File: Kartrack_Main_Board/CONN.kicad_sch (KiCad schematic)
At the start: 17 parts, among them J1 USB_C_Receptacle_USB2.0_14P, SW1 SW_Push, SW2 SW_Push, SW3 SW_Push

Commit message: pcb
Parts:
- added VEXTD1: Conn_01x02_Socket, Connector_Phoenix_MC:PhoenixContact_MC_1,5_2-G-3.81_1x02_P3.81mm_Horizontal, symbol Connector:Conn_01x02_Socket
- JP1: footprint (none) -> Jumper:SolderJumper-2_P1.3mm_Open_RoundedPad1.0x1.5mm
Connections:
- net GND: now also VEXTD1.2 (Pin_2)
- net at JP1.2 (B): now also VEXTD1.1 (Pin_1)
- net PF6_STBY_GPS renamed PF6
- net PG6 renamed PG6_STBY_GPS
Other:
- note added: "VEXT DISCO"
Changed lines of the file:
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@@
 		)
 	)
+	(text "VEXT DISCO\n"
+		(exclude_from_sim no)
+		(at 184.912 44.196 0)
+		(effects
+			(font
+				(size 1.27 1.27)
+			)
+		)
+	)
 	(junction
 		(at 55.88 113.03)
@@
 	(wire
 		(pts
-			(xy 186.69 54.61) (xy 186.69 55.88)
+			(xy 186.69 53.34) (xy 186.69 55.88)
 		)
 		(stroke
@@
 	(wire
 		(pts
+			(xy 179.07 53.34) (xy 186.69 53.34)
+		)
+		(stroke
+			(width 0)
+			(type default)
+		)
+	)
+	(wire
+		(pts
+			(xy 179.07 50.8) (xy 190.5 50.8)
+		)
+		(stroke
+			(width 0)
+			(type default)
+		)
+	)
+	(wire
+		(pts
 			(xy 194.31 57.15) (xy 194.31 66.04)
 		)
@@
 	(wire
 		(pts
+			(xy 190.5 50.8) (xy 190.5 52.07)
+		)
+		(stroke
+			(width 0)
+			(type default)
+		)
+	)
+	(wire
+		(pts
 			(xy 161.29 154.94) (xy 161.29 153.67)
 		)
@@
 		)
 	)
-	(hierarchical_label "PF6_STBY_GPS"
+	(hierarchical_label "PF6"
 		(shape input)
 		(at 201.93 104.14 0)
@@
 		)
 	)
-	(hierarchical_label "PG6"
+	(hierarchical_label "PG6_STBY_GPS"
 		(shape input)
 		(at 176.53 81.28 180)
@@
 	)
 	(symbol
+		(lib_id "Connector:Conn_01x02_Socket")
+		(at 173.99 53.34 180)
+		(unit 1)
+		(exclude_from_sim no)
+		(in_bom yes)
+		(on_board yes)
+		(dnp no)
+		(fields_autoplaced yes)
+		(property "Reference" "VEXTD1"
+			(at 174.625 45.72 0)
+			(effects
+				(font
+					(size 1.27 1.27)
+				)
+			)
+		)
+		(property "Value" "Conn_01x02_Socket"
+			(at 174.625 48.26 0)
+			(effects
+				(font
+					(size 1.27 1.27)
+				)
+			)
+		)
+		(property "Footprint" "Connector_Phoenix_MC:PhoenixContact_MC_1,5_2-G-3.81_1x02_P3.81mm_Horizontal"
+			(at 173.99 53.34 0)
+			(effects
+				(font
+					(size 1.27 1.27)
+				)
+				(hide yes)
+			)
+		)
+		(property "Datasheet" "~"
+			(at 173.99 53.34 0)
+			(effects
+				(font
+					(size 1.27 1.27)
+				)
+				(hide yes)
+			)
+		)
+		(property "Description" "Generic connector, single row, 01x02, script generated"
+			(at 173.99 53.34 0)
+			(effects
+				(font
+					(size 1.27 1.27)
+				)
+				(hide yes)
+			)
+		)
+		(pin "2"
+		)
+		(pin "1"
+		)
+		(instances
+			(project ""
+				(path "/7d0ecb76-dd3a-488e-b45e-ae217463e751/85ccdc23-ae17-49a7-b6f3-41d41d1b2e3d"
+					(reference "VEXTD1")
+					(unit 1)
+				)
+			)
+		)
+	)
+	(symbol
 		(lib_id "power:+3.3V")
 		(at 204.47 133.35 0)
@@
 	)
 	(symbol
-		(lib_id "power:VDD")
-		(at 186.69 54.61 0)
-		(unit 1)
-		(exclude_from_sim no)
-		(in_bom yes)
-		(on_board yes)
-		(dnp no)
-		(fields_autoplaced yes)
-		(property "Reference" "#PWR04"
-			(at 186.69 58.42 0)
-			(effects
-				(font
-					(size 1.27 1.27)
-				)
-				(hide yes)
-			)
-		)
-		(property "Value" "VEXT_DISCO"
-			(at 186.69 49.53 0)
-			(effects
-				(font
-					(size 1.27 1.27)
-				)
-			)
-		)
-		(property "Footprint" ""
-			(at 186.69 54.61 0)
-			(effects
-				(font
-					(size 1.27 1.27)
-				)
-				(hide yes)
-			)
-		)
-		(property "Datasheet" ""
-			(at 186.69 54.61 0)
-			(effects
-				(font
-					(size 1.27 1.27)
-				)
-				(hide yes)
-			)
-		)
-		(property "Description" "Power symbol creates a global label with name \"VDD\""
-			(at 186.69 54.61 0)
-			(effects
-				(font
-					(size 1.27 1.27)
-				)
-				(hide yes)
-			)
-		)
-		(pin "1"
-		)
-		(instances
-			(project ""
-				(path "/7d0ecb76-dd3a-488e-b45e-ae217463e751/85ccdc23-ae17-49a7-b6f3-41d41d1b2e3d"
-					(reference "#PWR04")
-					(unit 1)
-				)
-			)
-		)
-	)
-	(symbol
 		(lib_id "MCU_Module:Arduino_UNO_R3")
 		(at 189.23 91.44 0)
@@
 			)
 		)
-		(property "Footprint" ""
+		(property "Footprint" "Jumper:SolderJumper-2_P1.3mm_Open_RoundedPad1.0x1.5mm"
 			(at 186.69 59.69 0)
 			(effects
@@
 					(unit 1)
 				)
+			)
+		)
+	)
+	(symbol
+		(lib_id "power:GND")
+		(at 190.5 52.07 0)
+		(unit 1)
+		(exclude_from_sim no)
+		(in_bom yes)
+		(on_board yes)
+		(dnp no)
+		(fields_autoplaced yes)
+		(property "Reference" "#PWR04"
+			(at 190.5 58.42 0)
+			(effects
+				(font
+					(size 1.27 1.27)
+				)
+				(hide yes)
+			)
+		)
+		(property "Value" "GND"
+			(at 190.5 57.15 0)
+			(effects
+				(font
+					(size 1.27 1.27)
+				)
+			)
+		)
+		(property "Footprint" ""
+			(at 190.5 52.07 0)
+			(effects
+				(font
+					(size 1.27 1.27)
+				)
+				(hide yes)
+			)
+		)
+		(property "Datasheet" ""
+			(at 190.5 52.07 0)
+			(effects
+				(font
+					(size 1.27 1.27)
+				)
+				(hide yes)
+			)
+		)
+		(property "Description" "Power symbol creates a global label with name \"GND\" , ground"
+			(at 190.5 52.07 0)
+			(effects
+				(font
+					(size 1.27 1.27)
+				)
+				(hide yes)
+			)
+		)
+		(pin "1"
+		)
+		(instances
+			(project ""
+				(path "/7d0ecb76-dd3a-488e-b45e-ae217463e751/85ccdc23-ae17-49a7-b6f3-41d41d1b2e3d"
+					(reference "#PWR04")
+					(unit 1)
+				)

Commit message: PCB V1
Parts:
- removed J1: USB_C_Receptacle_USB2.0_14P, Connector_USB:USB_C_Receptacle_GCT_USB4125-xx-x-0190_6P_TopMnt_Horizontal, symbol Connector:USB_C_Receptacle_USB2.0_14P
- added J6: USB_C_Receptacle_PowerOnly_6P, Connector_USB:USB_C_Receptacle_GCT_USB4125-xx-x_6P_TopMnt_Horizontal, symbol Connector:USB_C_Receptacle_PowerOnly_6P
- added JP3: SolderJumper_2_Open, Jumper:SolderJumper-2_P1.3mm_Open_RoundedPad1.0x1.5mm, symbol Jumper:SolderJumper_2_Open
- SW1, SW2, SW3: footprint Connector_PinSocket_2.54mm:PinSocket_1x02_P2.54mm_Vertical_SMD_Pin1Left -> Connector_JST:JST_PH_S2B-PH-K_1x02_P2.00mm_Horizontal
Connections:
- net +5V: now also J6.A9 (VBUS), J6.B9 (VBUS), JP3.2 (B); no longer A2.5 (+5V)
- net GND: now also J6.A12 (GND), J6.B12 (GND), J6.S1 (SHIELD)
- net at R1.1: now also J6.A5 (CC1)
- net at R2.1: now also J6.B5 (CC2)
- new net: A2.5 (+5V), JP3.1 (A)
- no-connect marks 10 -> 6
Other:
- moved on the sheet: R1, R2

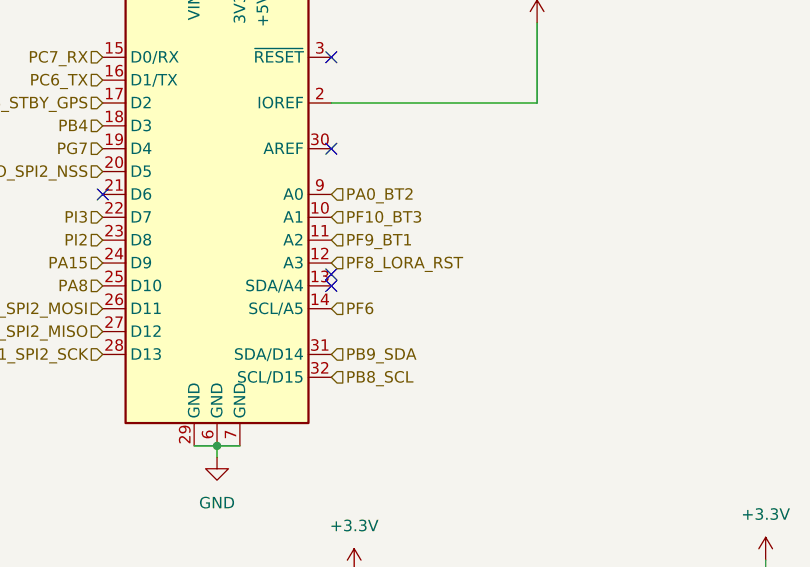
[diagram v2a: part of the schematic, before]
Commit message: add adc batt
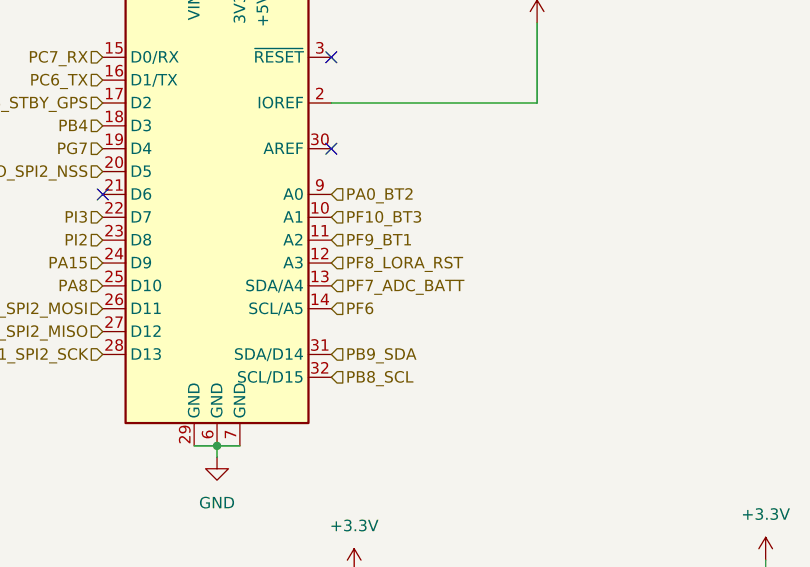
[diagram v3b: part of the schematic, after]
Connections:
- net PF7_ADC_BATT: now reaches A2.13 (SDA/A4)
- no-connect marks 6 -> 4
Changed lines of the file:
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@@
-	)
-	(no_connect
-		(at 201.93 101.6)
 	)
 	(no_connect
 		(at 201.93 86.36)
-	)
-	(no_connect
-		(at 201.93 100.33)
 	)
 	(wire
@@
 		(effects
 			(font
+				(size 1.27 1.27)
+			)
+			(justify left)
+		)
+	)
+	(hierarchical_label "PF7_ADC_BATT"
+		(shape input)
+		(at 201.93 101.6 0)
+		(effects
+			(font

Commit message: Alim jumper
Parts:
- removed JP3: SolderJumper_2_Open, Jumper:SolderJumper-2_P1.3mm_Open_RoundedPad1.0x1.5mm, symbol Jumper:SolderJumper_2_Open
- added JP4: SolderJumper_3_Open, Jumper:SolderJumper-3_P2.0mm_Open_TrianglePad1.0x1.5mm_NumberLabels, symbol Jumper:SolderJumper_3_Open
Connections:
- net +5V: now also JP4.1 (A)
- net at A2.5 (+5V): now also JP4.3 (B)
- net at A2.8 (VIN), JP1.1 (A): now also JP4.2 (C)
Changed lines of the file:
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@@
+	)
+	(junction
+		(at 186.69 64.77)
+		(diameter 0)
+		(color 0 0 0 0)
 	)
 	(junction
@@
 	(wire
 		(pts
+			(xy 186.69 64.77) (xy 190.5 64.77)
+		)
+		(stroke
+			(width 0)
+			(type default)
+		)
+	)
+	(wire
+		(pts
 			(xy 229.87 142.24) (xy 236.22 142.24)
 		)
@@
 	(wire
 		(pts
+			(xy 186.69 64.77) (xy 186.69 66.04)
+		)
+		(stroke
+			(width 0)
+			(type default)
+		)
+	)
+	(wire
+		(pts
 			(xy 142.24 142.24) (xy 147.32 142.24)
 		)
@@
 	(wire
 		(pts
+			(xy 194.31 64.77) (xy 194.31 66.04)
+		)
+		(stroke
+			(width 0)
+			(type default)
+		)
+	)
+	(wire
+		(pts
 			(xy 189.23 119.38) (xy 189.23 120.65)
 		)
@@
 	(wire
 		(pts
-			(xy 194.31 50.8) (xy 194.31 55.88)
+			(xy 186.69 63.5) (xy 186.69 64.77)
 		)
 		(stroke
@@
 	(wire
 		(pts
+			(xy 190.5 59.69) (xy 190.5 64.77)
+		)
+		(stroke
+			(width 0)
+			(type default)
+		)
+	)
+	(wire
+		(pts
 			(xy 186.69 119.38) (xy 189.23 119.38)
 		)
@@
 	(wire
 		(pts
-			(xy 186.69 63.5) (xy 186.69 66.04)
-		)
-		(stroke
-			(width 0)
-			(type default)
-		)
-	)
-	(wire
-		(pts
 			(xy 68.58 67.31) (xy 69.85 67.31)
 		)
@@
 	(wire
 		(pts
-			(xy 194.31 63.5) (xy 194.31 66.04)
-		)
-		(stroke
-			(width 0)
-			(type default)
-		)
-	)
-	(wire
-		(pts
 			(xy 204.47 143.51) (xy 204.47 144.78)
 		)
@@
 		(pts
 			(xy 154.94 142.24) (xy 161.29 142.24)
+		)
+		(stroke
+			(width 0)
+			(type default)
+		)
+	)
+	(wire
+		(pts
+			(xy 194.31 50.8) (xy 194.31 54.61)
 		)
 		(stroke
@@
 	)
 	(symbol
+		(lib_id "Jumper:SolderJumper_3_Open")
+		(at 194.31 59.69 270)
+		(unit 1)
+		(exclude_from_sim yes)
+		(in_bom no)
+		(on_board yes)
+		(dnp no)
+		(fields_autoplaced yes)
+		(property "Reference" "JP4"
+			(at 196.85 58.4199 90)
+			(effects
+				(font
+					(size 1.27 1.27)
+				)
+				(justify left)
+			)
+		)
+		(property "Value" "SolderJumper_3_Open"
+			(at 196.85 60.9599 90)
+			(effects
+				(font
+					(size 1.27 1.27)
+				)
+				(justify left)
+			)
+		)
+		(property "Footprint" "Jumper:SolderJumper-3_P2.0mm_Open_TrianglePad1.0x1.5mm_NumberLabels"
+			(at 194.31 59.69 0)
+			(effects
+				(font
+					(size 1.27 1.27)
+				)
+				(hide yes)
+			)
+		)
+		(property "Datasheet" "~"
+			(at 194.31 59.69 0)
+			(effects
+				(font
+					(size 1.27 1.27)
+				)
+				(hide yes)
+			)
+		)
+		(property "Description" "Solder Jumper, 3-pole, open"
+			(at 194.31 59.69 0)
+			(effects
+				(font
+					(size 1.27 1.27)
+				)
+				(hide yes)
+			)
+		)
+		(pin "3"
+		)
+		(pin "2"
+		)
+		(pin "1"
+		)
+		(instances
+			(project ""
+				(path "/7d0ecb76-dd3a-488e-b45e-ae217463e751/85ccdc23-ae17-49a7-b6f3-41d41d1b2e3d"
+					(reference "JP4")
+					(unit 1)
+				)
+			)
+		)
+	)
+	(symbol
 		(lib_id "Device:C_Small")
 		(at 236.22 148.59 0)
@@
 					(unit 1)
 				)
-			)
-		)
-	)
-	(symbol
-		(lib_id "Jumper:SolderJumper_2_Open")
-		(at 194.31 59.69 90)
-		(unit 1)
-		(exclude_from_sim yes)
-		(in_bom no)
-		(on_board yes)
-		(dnp no)
-		(property "Reference" "JP3"
-			(at 188.976 59.69 90)
-			(effects
-				(font
-					(size 1.27 1.27)
-				)
-				(justify right)
-			)
-		)
-		(property "Value" "SolderJumper_2_Open"
-			(at 167.132 60.96 90)
-			(effects
-				(font
-					(size 1.27 1.27)
-				)
-				(justify right)
-				(hide yes)
-			)
-		)
-		(property "Footprint" "Jumper:SolderJumper-2_P1.3mm_Open_RoundedPad1.0x1.5mm"
-			(at 194.31 59.69 0)
-			(effects
-				(font
-					(size 1.27 1.27)
-				)
-				(hide yes)
-			)
-		)
-		(property "Datasheet" "~"
-			(at 194.31 59.69 0)
-			(effects
-				(font
-					(size 1.27 1.27)
-				)
-				(hide yes)
-			)
-		)
-		(property "Description" "Solder Jumper, 2-pole, open"
-			(at 194.31 59.69 0)
-			(effects
-				(font
-					(size 1.27 1.27)
-				)
-				(hide yes)
-			)
-		)
-		(property "Manufacturer_Part_Number" ""
-			(at 194.31 59.69 0)
-			(effects
-				(font
-					(size 1.27 1.27)
-				)
-			)
-		)
-		(pin "2"
-		)
-		(pin "1"
-		)
-		(instances
-			(project "Kartrack_Main_Board"
-				(path "/7d0ecb76-dd3a-488e-b45e-ae217463e751/85ccdc23-ae17-49a7-b6f3-41d41d1b2e3d"
-					(reference "JP3")
-					(unit 1)
-				)
